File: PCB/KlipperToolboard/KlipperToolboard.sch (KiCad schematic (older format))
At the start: 51 parts, among them J1 Endstop, J2 Servo, J3 HeaterThermistor, J4 PartFan, J5 HeaterFan, J6 Heater, J7 Conn_02x03_Counter_Clockwise, J8 PWRUART, J9 Stepper, Q1 AO3400A, Q2 AO3400A, Q3 WSF3085, U1 ATmega168A-AU, U2 TMC2209-LA, Y1 16Mhz

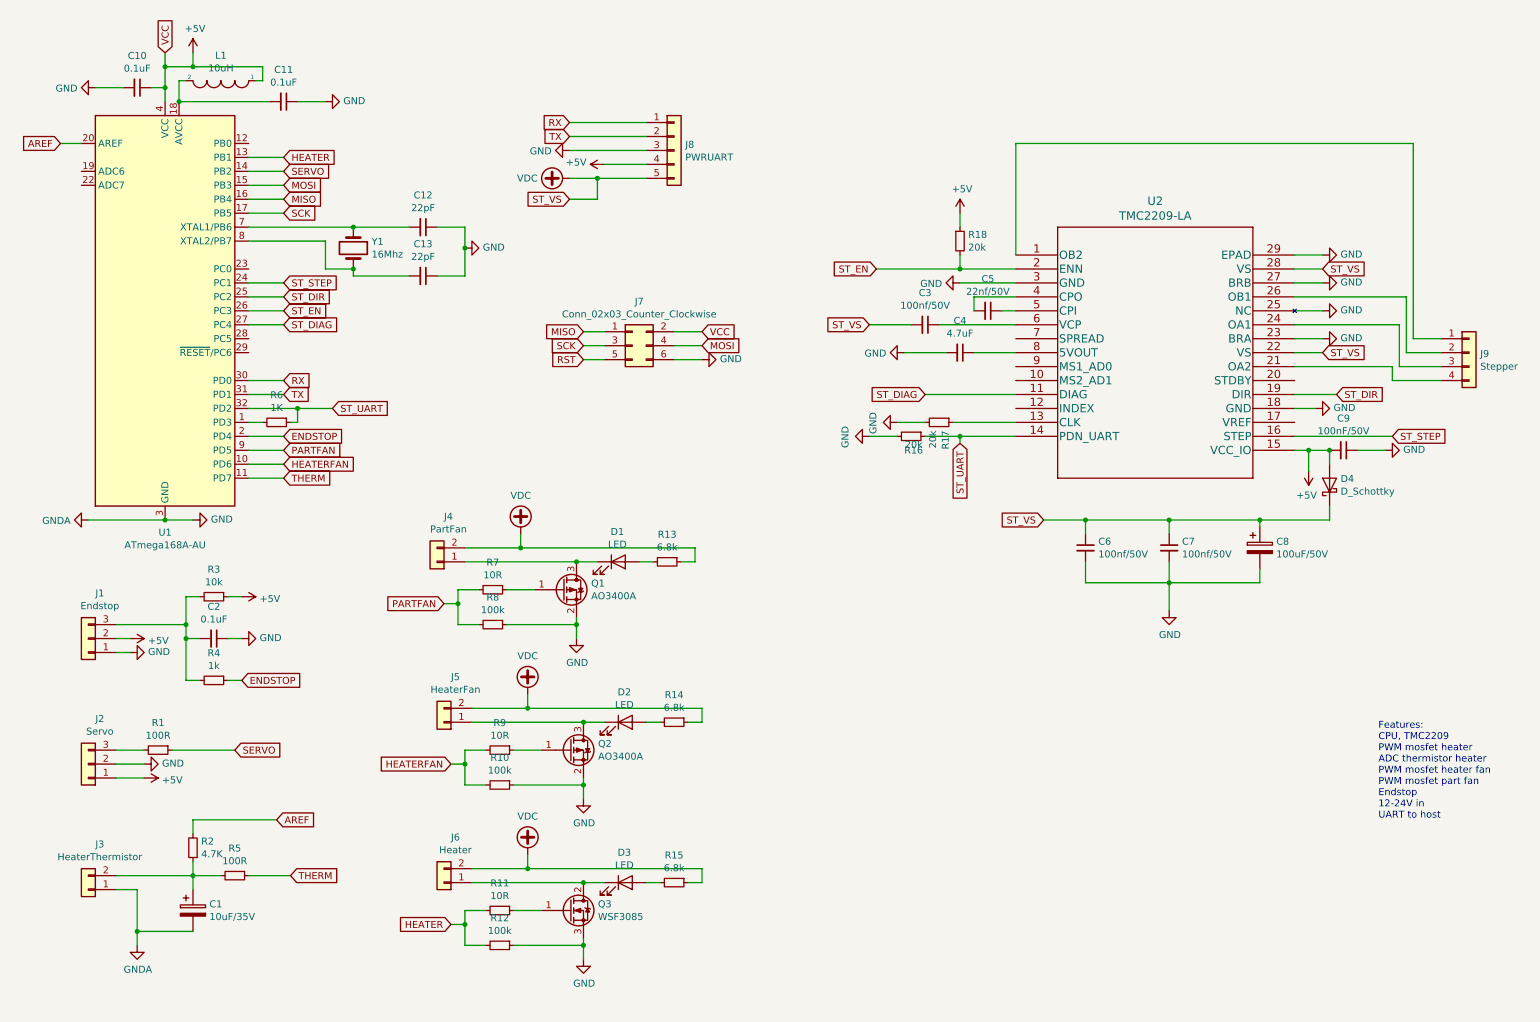
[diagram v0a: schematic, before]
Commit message: Changed to STM32
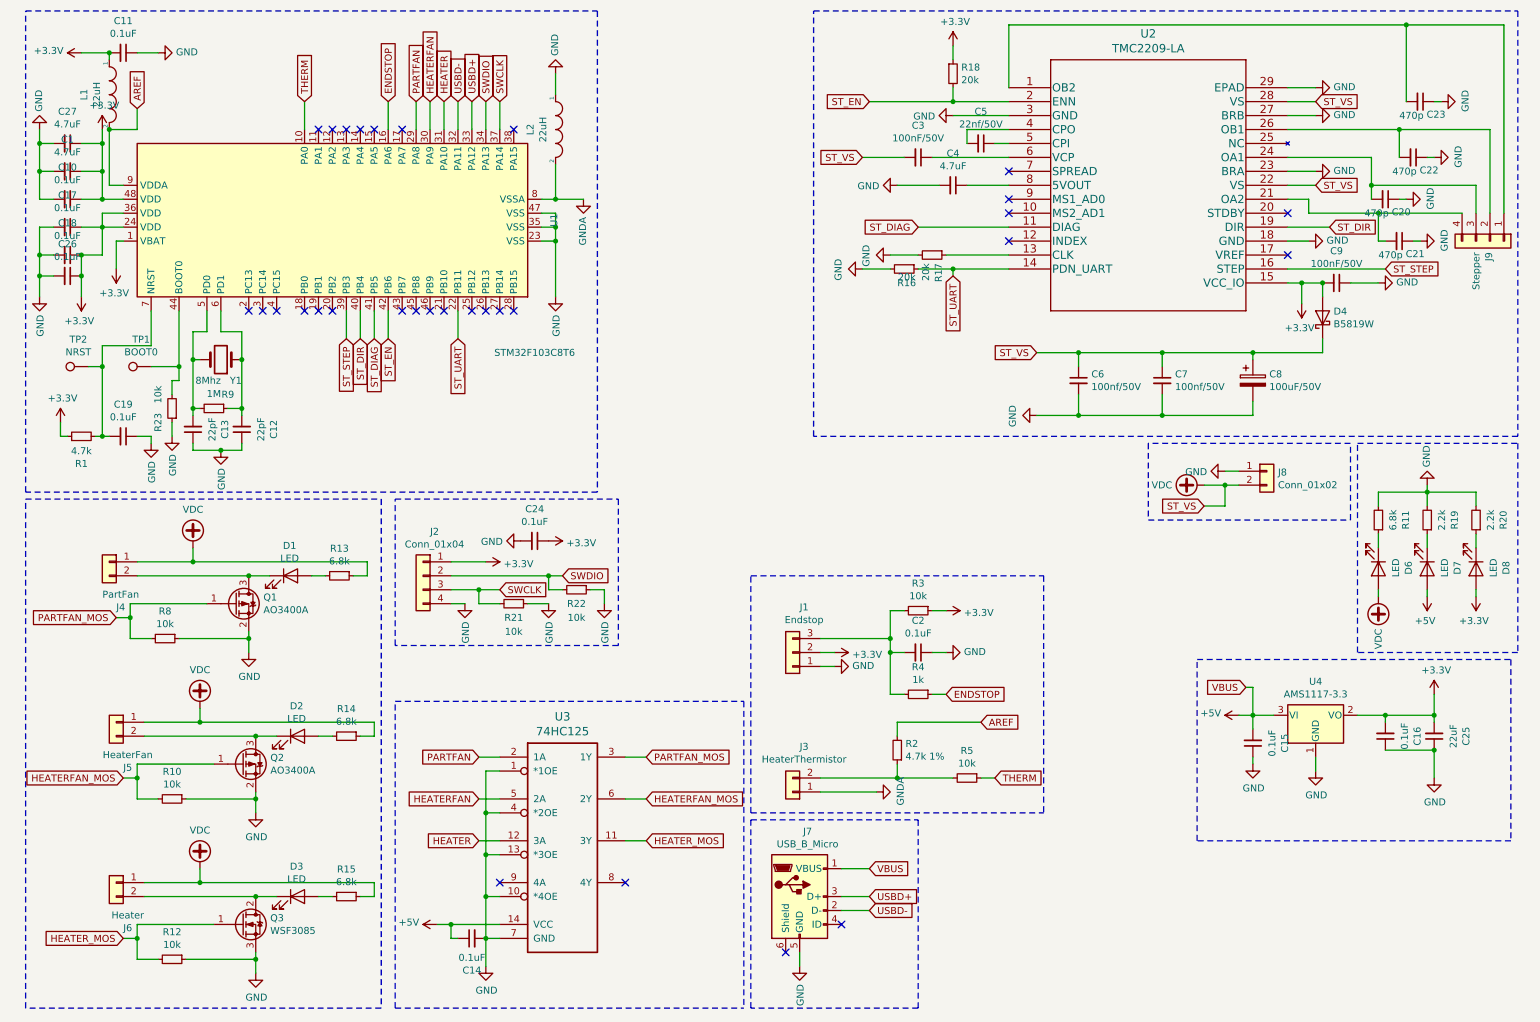
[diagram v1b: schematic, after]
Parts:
- removed C1: 10uF/35V, Capacitor_SMD:CP_Elec_6.3x5.8, symbol Device:CP
- removed J2: Servo, Connector_JST:JST_EH_B3B-EH-A_1x03_P2.50mm_Vertical, symbol Connector_Generic:Conn_01x03
- removed J7: Conn_02x03_Counter_Clockwise, Connector_PinHeader_2.54mm:PinHeader_2x03_P2.54mm_Vertical, symbol Connector_Generic:Conn_02x03_Odd_Even
- removed J8: PWRUART, Connector_Molex:Molex_KK-254_AE-6410-05A_1x05_P2.54mm_Vertical, symbol Connector_Generic:Conn_01x05
- removed R6: 1K, Resistor_SMD:R_0603_1608Metric, symbol Device:R_Small
- removed R7: 10R, Resistor_SMD:R_0603_1608Metric, symbol Device:R_Small
- removed U1: ATmega168A-AU, Package_QFP:TQFP-32_7x7mm_P0.8mm, symbol MCU_Microchip_ATmega:ATmega168A-AU
- added C1, C27: 4.7uF, Capacitor_SMD:C_0603_1608Metric, symbol Device:C_Small
- added C14, C15, C16, C17, C18, C19, C24, C26: 0.1uF, Capacitor_SMD:C_0603_1608Metric, symbol Device:C_Small
- added C20, C21, C22, C23: 470p, Capacitor_SMD:C_0603_1608Metric, symbol Device:C_Small
- added C25: 22uF, Capacitor_SMD:C_0603_1608Metric, symbol Device:C_Small
- added D6, D7, D8: LED, LED_SMD:LED_0603_1608Metric, symbol Device:LED
- added J2: Conn_01x04, KlipperToolboard:Testpad 02x02 2.54, symbol Connector_Generic:Conn_01x04
- added J7: USB_B_Micro, Connector_USB:USB_Micro-B_Molex-105017-0001, symbol Connector:USB_B_Micro
- added J8: Conn_01x02, Connector_Molex:Molex_Micro-Fit_3.0_43650-0200_1x02_P3.00mm_Horizontal, symbol Connector_Generic:Conn_01x02
- added L2: 22uH, Inductor_SMD:L_1206_3216Metric, symbol pspice:INDUCTOR
- added R19, R20: 2.2k, Resistor_SMD:R_0603_1608Metric, symbol Device:R_Small
- added R21, R22, R23: 10k, Resistor_SMD:R_0603_1608Metric, symbol Device:R_Small
- added TP1: BOOT0, TestPoint:TestPoint_Pad_D1.5mm, symbol Connector:TestPoint
- added TP2: NRST, TestPoint:TestPoint_Pad_D1.5mm, symbol Connector:TestPoint
- added U1: STM32F103C8T6, Package_QFP:LQFP-48_7x7mm_P0.5mm, symbol MCU_ST_STM32F1:STM32F103C8Tx
- added U3: 74HC125, Package_SO:SOIC-14_3.9x8.7mm_P1.27mm, symbol mfk_74xx:74HC125
- added U4: AMS1117-3.3, Package_TO_SOT_SMD:SOT-223-3_TabPin2, symbol Regulator_Linear:AMS1117-3.3
- C3: value 100nf/50V -> 100nF/50V
- C8: LCSC Part # (none) -> C176665
- D4: value D_Schottky -> B5819W; LCSC Part # (none) -> C8598
- J1: footprint Connector_JST:JST_EH_B3B-EH-A_1x03_P2.50mm_Vertical -> Connector_JST:JST_EH_S3B-EH_1x03_P2.50mm_Horizontal
- J3: footprint Connector_JST:JST_EH_B2B-EH-A_1x02_P2.50mm_Vertical -> Connector_JST:JST_EH_S2B-EH_1x02_P2.50mm_Horizontal
- J4, J5, J6: footprint Connector_JST:JST_EH_B2B-EH-A_1x02_P2.50mm_Vertical -> TerminalBlock_TE-Connectivity:TerminalBlock_TE_282834-2_1x02_P2.54mm_Horizontal
- J9: footprint Connector_Molex:Molex_KK-254_AE-6410-04A_1x04_P2.54mm_Vertical -> Connector_JST:JST_EH_S4B-EH_1x04_P2.50mm_Horizontal
- L1: value 10uH -> 22uH
- Q1, Q2: LCSC Part # (none) -> C20917
- Q3: LCSC Part # (none) -> C148428
- R1: value 100R -> 4.7k
- R10, R12, R8: value 100k -> 10k
- R11: value 10R -> 6.8k
- R2: value 4.7K -> 4.7k 1%
- R5: value 100R -> 10k
- R9: value 10R -> 1M
- U2: LCSC Part # (none) -> C465949
- Y1: value 16Mhz -> 8Mhz; LCSC Part # (none) -> C115962
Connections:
- net SERVO is gone; now on net +3V3: R1.1
- net +5V: now also C14.1, C15.2, D7.2 (A), J7.1 (VBUS), U3.14 (VCC), U4.3 (VI); no longer C10.1, C9.2, D4.2 (A), J1.2 (Pin_2), L1.1, R18.1, R3.1, U2.15 (VCC_IO)
- net AREF: now also L1.2, U1.9 (VDDA)
- net ENDSTOP: now also U1.16 (PA6)
- net GND: now also R11.2, C1.2, C14.2, C15.1, C16.1, C17.2, C18.2, C19.1, C20.1, C21.1, C22.1, C23.1, C24.2, C25.1, C26.2, C27.2, J2.4 (Pin_4), J7.5 (GND), J8.1 (Pin_1), L2.1, R19.2, R20.2, R21.1, R22.1, R23.1, U1.23 (VSS), U1.35 (VSS), U1.47 (VSS), U3.1 (*1OE), U3.10 (*4OE), U3.13 (*3OE), U3.4 (*2OE), U3.7 (GND), U4.1 (GND); no longer J3.1 (Pin_1), U2.25 (NC)
- net HEATER: now also U1.31 (PA10), U3.12 (3A); no longer R11.2, R12.2
- net HEATERFAN: now also U1.30 (PA9), U3.5 (2A); no longer R10.2, R9.2
- net PARTFAN: now also U1.29 (PA8), U3.2 (1A); no longer R8.2
- net ST_DIAG: now also U1.41 (PB5)
- net ST_DIR: now also U1.40 (PB4)
- net ST_EN: now also U1.42 (PB6)
- net ST_STEP: now also U1.39 (PB3)
- net ST_UART: now also U1.22 (PB11)
- net THERM: now also U1.10 (PA0)
- net VDC: now also J4.1 (Pin_1), J5.1 (Pin_1), J6.1 (Pin_1), D6.2 (A), J8.2 (Pin_2); no longer J4.2 (Pin_2), J5.2 (Pin_2), J6.2 (Pin_2)
- net at J9.1 (Pin_1), U2.1 (OB2): now also C23.2
- net at J9.4 (Pin_4), U2.21 (OA2): now also C21.2
- net at J9.3 (Pin_3), U2.24 (OA1): now also C20.2
- net at J9.2 (Pin_2), U2.26 (OB1): now also C22.2
- net +3V3: now reaches C11.2
- net +3V3: now also C10.1, C9.2, D4.2 (A), J1.2 (Pin_2), L1.1, R18.1, R3.1, U2.15 (VCC_IO), C1.1, C16.2, C17.1, C18.1, C24.1, C25.2, C26.1, C27.1, D8.2 (A), J2.1 (Pin_1), U1.1 (VBAT), U1.24 (VDD), U1.36 (VDD), U1.48 (VDD), U4.2 (VO); no longer L1.2
- net at C12.2, Y1.1: now also R9.1, U1.6 (PD1)
- net at C13.2, Y1.2: now also R9.2, U1.5 (PD0)
- net at D1.1 (K), Q1.3 (D): now also J4.2 (Pin_2); no longer J4.1 (Pin_1)
- net at D2.1 (K), Q2.3 (D): now also J5.2 (Pin_2); no longer J5.1 (Pin_1)
- net at D3.1 (K), Q3.2 (D): now also J6.2 (Pin_2); no longer J6.1 (Pin_1)
- net at R1.2: now also C19.2, TP2.1, U1.7 (NRST)
- net PARTFAN_MOS: now reaches Q1.1 (G)
- net PARTFAN_MOS: now also R8.2, U3.3 (1Y)
- net HEATERFAN_MOS: now reaches Q2.1 (G)
- net HEATERFAN_MOS: now also R10.2, U3.6 (2Y); no longer R9.1
- net at R11.1: now also D6.1 (K); no longer Q3.1 (G)
- new net: R23.2, TP1.1, U1.44 (BOOT0)
- new net: D7.1 (K), R19.1
- new net: D8.1 (K), R20.1
- new net GNDA: J3.1 (Pin_1), L2.2, U1.8 (VSSA)
- new net HEATER_MOS: Q3.1 (G), R12.2, U3.11 (3Y)
- new net SWCLK: J2.3 (Pin_3), R21.2, U1.37 (PA14)
- new net SWDIO: J2.2 (Pin_2), R22.2, U1.34 (PA13)
- new net USBD+: J7.3 (D+), U1.33 (PA12)
- new net USBD-: J7.2 (D-), U1.32 (PA11)
- no-connect marks 0 -> 31
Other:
- note removed: "Features: \nCPU, TMC2209\nPWM mosfet heater\nADC thermistor heater\nPWM mosfet heater fan\nPWM mosfet part fan\nEndstop\n12-24V in\nUART to host\n"
- moved on the sheet: C11, C12, C13, C2, C3, C4, C5, C6, C7, C8, C9, D1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

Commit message: Change to STM32 and CAN Bus
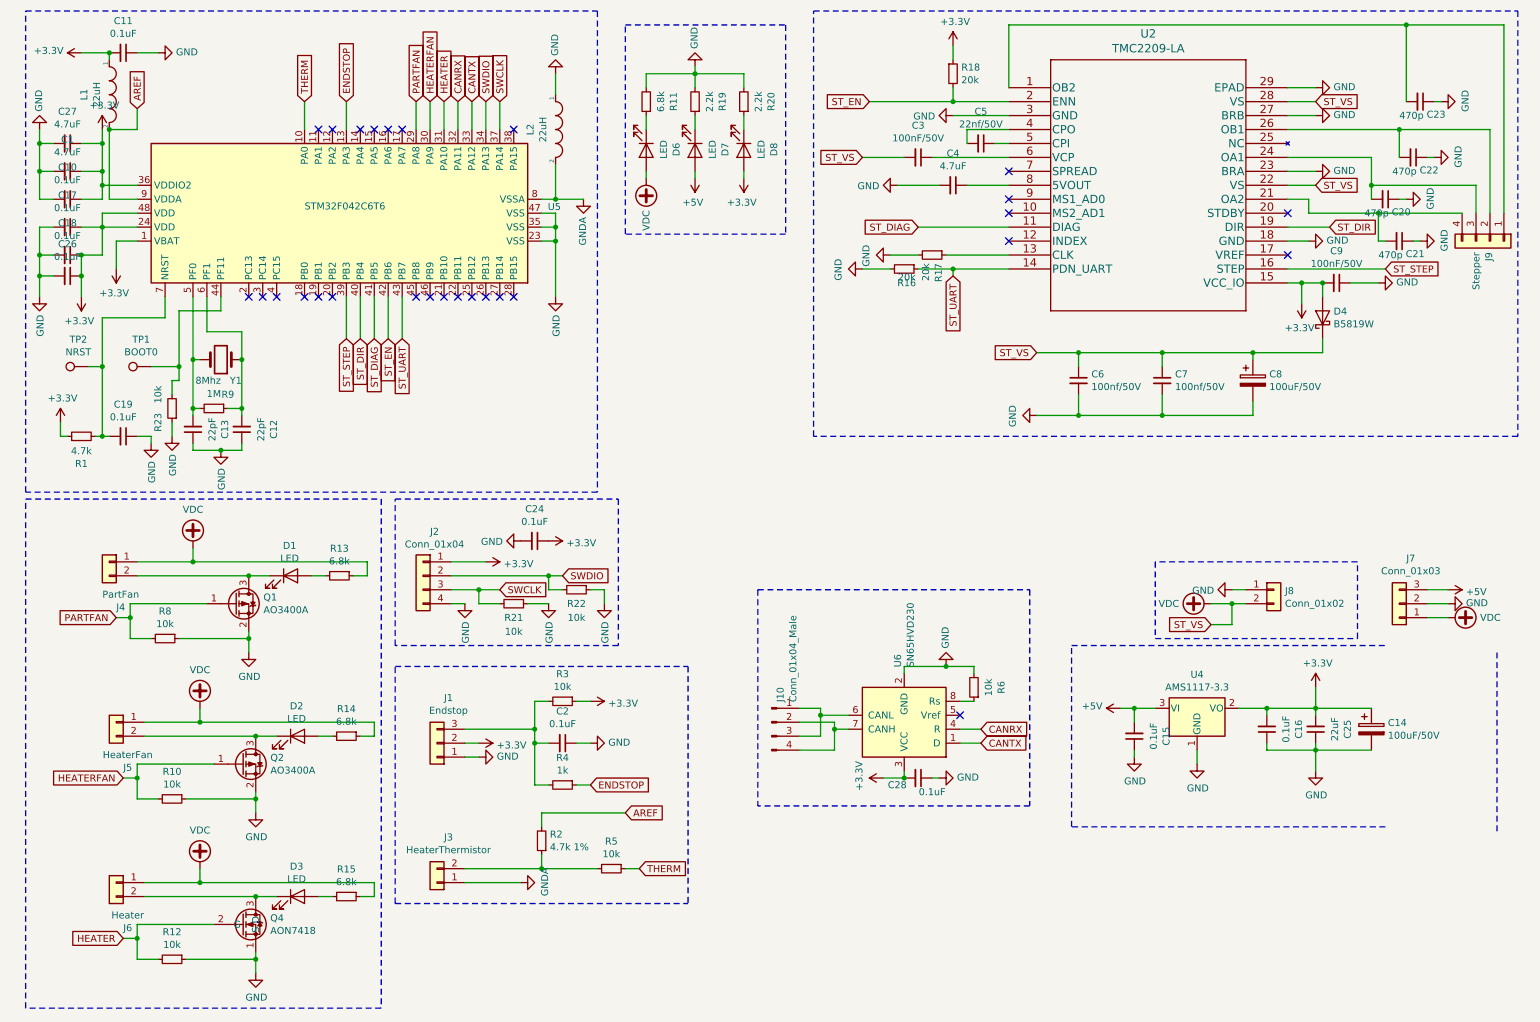
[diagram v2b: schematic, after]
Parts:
- removed C14: 0.1uF, Capacitor_SMD:C_0603_1608Metric, symbol Device:C_Small
- removed J7: USB_B_Micro, Connector_USB:USB_Micro-B_Molex-105017-0001, symbol Connector:USB_B_Micro
- removed Q3: WSF3085, Package_TO_SOT_SMD:TO-252-2, symbol Transistor_FET:QM6006D
- removed U1: STM32F103C8T6, Package_QFP:LQFP-48_7x7mm_P0.5mm, symbol MCU_ST_STM32F1:STM32F103C8Tx
- removed U3: 74HC125, Package_SO:SOIC-14_3.9x8.7mm_P1.27mm, symbol mfk_74xx:74HC125
- added C14: 100uF/50V, Capacitor_Tantalum_SMD:CP_EIA-3528-12_Kemet-T, symbol Device:CP
- added C28: 0.1uF, Capacitor_SMD:C_0603_1608Metric, symbol Device:C_Small
- added J10: Conn_01x04_Male, KlipperToolboard:JST-ZH-THRx4, symbol Connector:Conn_01x04_Male
- added J7: Conn_01x03, Connector_PinHeader_2.54mm:PinHeader_1x03_P2.54mm_Vertical, symbol Connector_Generic:Conn_01x03
- added Q4: AON7418, KlipperToolboard:DFN-8-1EP_3x3mm_P0.65mm_EP1.7x2.05mm, symbol KlipperToolboard:AON7418
- added R6: 10k, Resistor_SMD:R_0603_1608Metric, symbol Device:R_Small
- added U5: STM32F042C6T6, Package_QFP:LQFP-48_7x7mm_P0.5mm, symbol MCU_ST_STM32F0:STM32F042C6Tx
- added U6: SN65HVD230, Package_SO:SOIC-8_3.9x4.9mm_P1.27mm, symbol Interface_CAN_LIN:SN65HVD230
- J2: footprint KlipperToolboard:Testpad 02x02 2.54 -> Connector_PinHeader_2.54mm:PinHeader_2x02_P2.54mm_Vertical
- L1, L2: footprint Inductor_SMD:L_1206_3216Metric -> Inductor_SMD:L_0805_2012Metric; LCSC Part # (none) -> C32375
- TP1, TP2: footprint TestPoint:TestPoint_Pad_D1.5mm -> Connector_PinHeader_2.54mm:PinHeader_1x01_P2.54mm_Vertical
- U4: LCSC Part # (none) -> C6186
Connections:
- net HEATERFAN_MOS is gone; now on net HEATERFAN: Q2.1 (G), R10.2
- net HEATER_MOS is gone; now on net HEATER: R12.2
- net PARTFAN_MOS is gone; now on net PARTFAN: Q1.1 (G), R8.2
- net +3V3: now also C14.1, C28.2, U5.1 (VBAT), U5.24 (VDD), U5.36 (VDDIO2), U5.48 (VDD), U6.3 (VCC)
- net +5V: now also J7.3 (Pin_3)
- net AREF: now also U5.9 (VDDA)
- net ENDSTOP: now also U5.13 (PA3)
- net GND: now also C14.2, C28.1, J7.2 (Pin_2), Q4.1 (S), R6.2, U5.23 (VSS), U5.35 (VSS), U5.47 (VSS), U6.2 (GND)
- net GNDA: now also U5.8 (VSSA)
- net HEATER: now also Q4.2 (G), U5.31 (PA10)
- net HEATERFAN: now also U5.30 (PA9)
- net PARTFAN: now also U5.29 (PA8)
- net ST_DIAG: now also U5.41 (PB5)
- net ST_DIR: now also U5.40 (PB4)
- net ST_EN: now also U5.42 (PB6)
- net ST_STEP: now also U5.39 (PB3)
- net ST_UART: now also U5.43 (PB7)
- net SWCLK: now also U5.37 (PA14)
- net SWDIO: now also U5.34 (PA13)
- net THERM: now also U5.10 (PA0)
- net VDC: now also J7.1 (Pin_1)
- net at D3.1 (K), J6.2 (Pin_2): now also Q4.3 (D)
- net at R23.2, TP1.1: now also U5.44 (PF11)
- net at C13.2, R9.2, Y1.2: now also U5.5 (PF0)
- net at C12.2, R9.1, Y1.1: now also U5.6 (PF1)
- net at C19.2, R1.2, TP2.1: now also U5.7 (NRST)
- new net: J10.1 (Pin_1), J10.3 (Pin_3), U6.6 (CANL)
- new net: J10.2 (Pin_2), J10.4 (Pin_4), U6.7 (CANH)
- new net: R6.1, U6.8 (Rs)
- new net CANRX: U5.32 (PA11), U6.4 (R)
- new net CANTX: U5.33 (PA12), U6.1 (D)
- no-connect marks 31 -> 28
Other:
- moved on the sheet: C15, C16, C2, C25, D6, D7, D8, J1, J3, J8, R11, R19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

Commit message: Tweaks and 3d models
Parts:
- J4, J5, J6: footprint TerminalBlock_TE-Connectivity:TerminalBlock_TE_282834-2_1x02_P2.54mm_Horizontal -> KlipperToolboard:TerminalBlock_TE_282834-2_1x02_P2.54mm_Horizontal
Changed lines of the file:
@@
 F 0 "J4" H 1018 4175 50  0000 C CNN
 F 1 "PartFan" H 1018 4266 50  0000 C CNN
-F 2 "TerminalBlock_TE-Connectivity:TerminalBlock_TE_282834-2_1x02_P2.54mm_Horizontal" H 1100 4500 50  0001 C CNN
+F 2 "KlipperToolboard:TerminalBlock_TE_282834-2_1x02_P2.54mm_Horizontal" H 1100 4500 50  0001 C CNN
 F 3 "~" H 1100 4500 50  0001 C CNN
 	1    1100 4500
@@
 F 0 "J5" H 1068 5325 50  0000 C CNN
 F 1 "HeaterFan" H 1068 5416 50  0000 C CNN
-F 2 "TerminalBlock_TE-Connectivity:TerminalBlock_TE_282834-2_1x02_P2.54mm_Horizontal" H 1150 5650 50  0001 C CNN
+F 2 "KlipperToolboard:TerminalBlock_TE_282834-2_1x02_P2.54mm_Horizontal" H 1150 5650 50  0001 C CNN
 F 3 "~" H 1150 5650 50  0001 C CNN
 	1    1150 5650
@@
 F 0 "J6" H 1068 6475 50  0000 C CNN
 F 1 "Heater" H 1068 6566 50  0000 C CNN
-F 2 "TerminalBlock_TE-Connectivity:TerminalBlock_TE_282834-2_1x02_P2.54mm_Horizontal" H 1150 6800 50  0001 C CNN
+F 2 "KlipperToolboard:TerminalBlock_TE_282834-2_1x02_P2.54mm_Horizontal" H 1150 6800 50  0001 C CNN
 F 3 "~" H 1150 6800 50  0001 C CNN
 	1    1150 6800
